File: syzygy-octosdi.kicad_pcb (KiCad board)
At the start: 2 copper layers, 50 x 100 mm, 211 parts, among them CN1 QTH-020-01-F-D-DP-A, J1 Conn_Coaxial, J2 Conn_Coaxial, J3 Conn_Coaxial, J4 Conn_Coaxial, J5 Conn_Coaxial, J6 Conn_Coaxial, J7 Conn_Coaxial, J8 Conn_Coaxial, J9 Conn_02x03_Odd_Even, U1 LMH0344SQE_NOPB, U10 GS2988-INE3, U11 STM32G031G8Ux, U2 LMH0344SQE_NOPB, U3 LMH0344SQE_NOPB, U4 LMH0344SQE_NOPB, U5 PCAL6416AHF, U6 PCAL6416AHF, U7 GS2988-INE3, U8 GS2988-INE3, U9 GS2988-INE3, X1 SX7DF148_500B20F30DNN

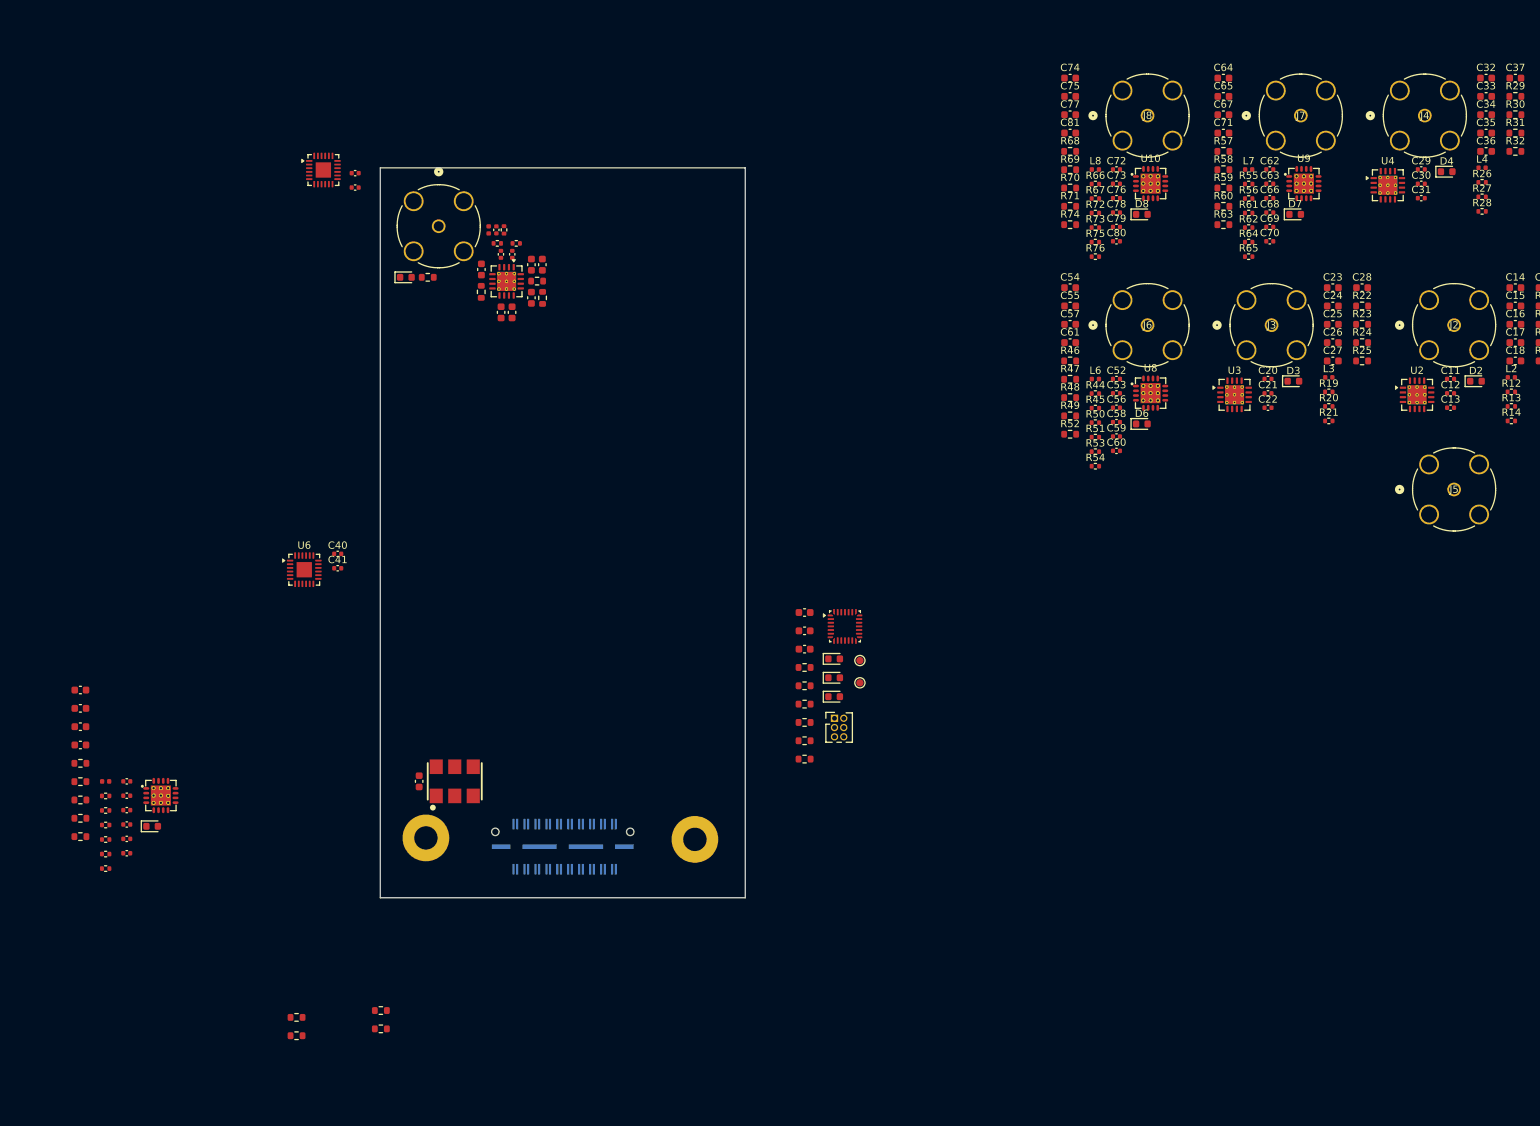
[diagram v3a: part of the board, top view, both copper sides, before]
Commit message: start laying out channels
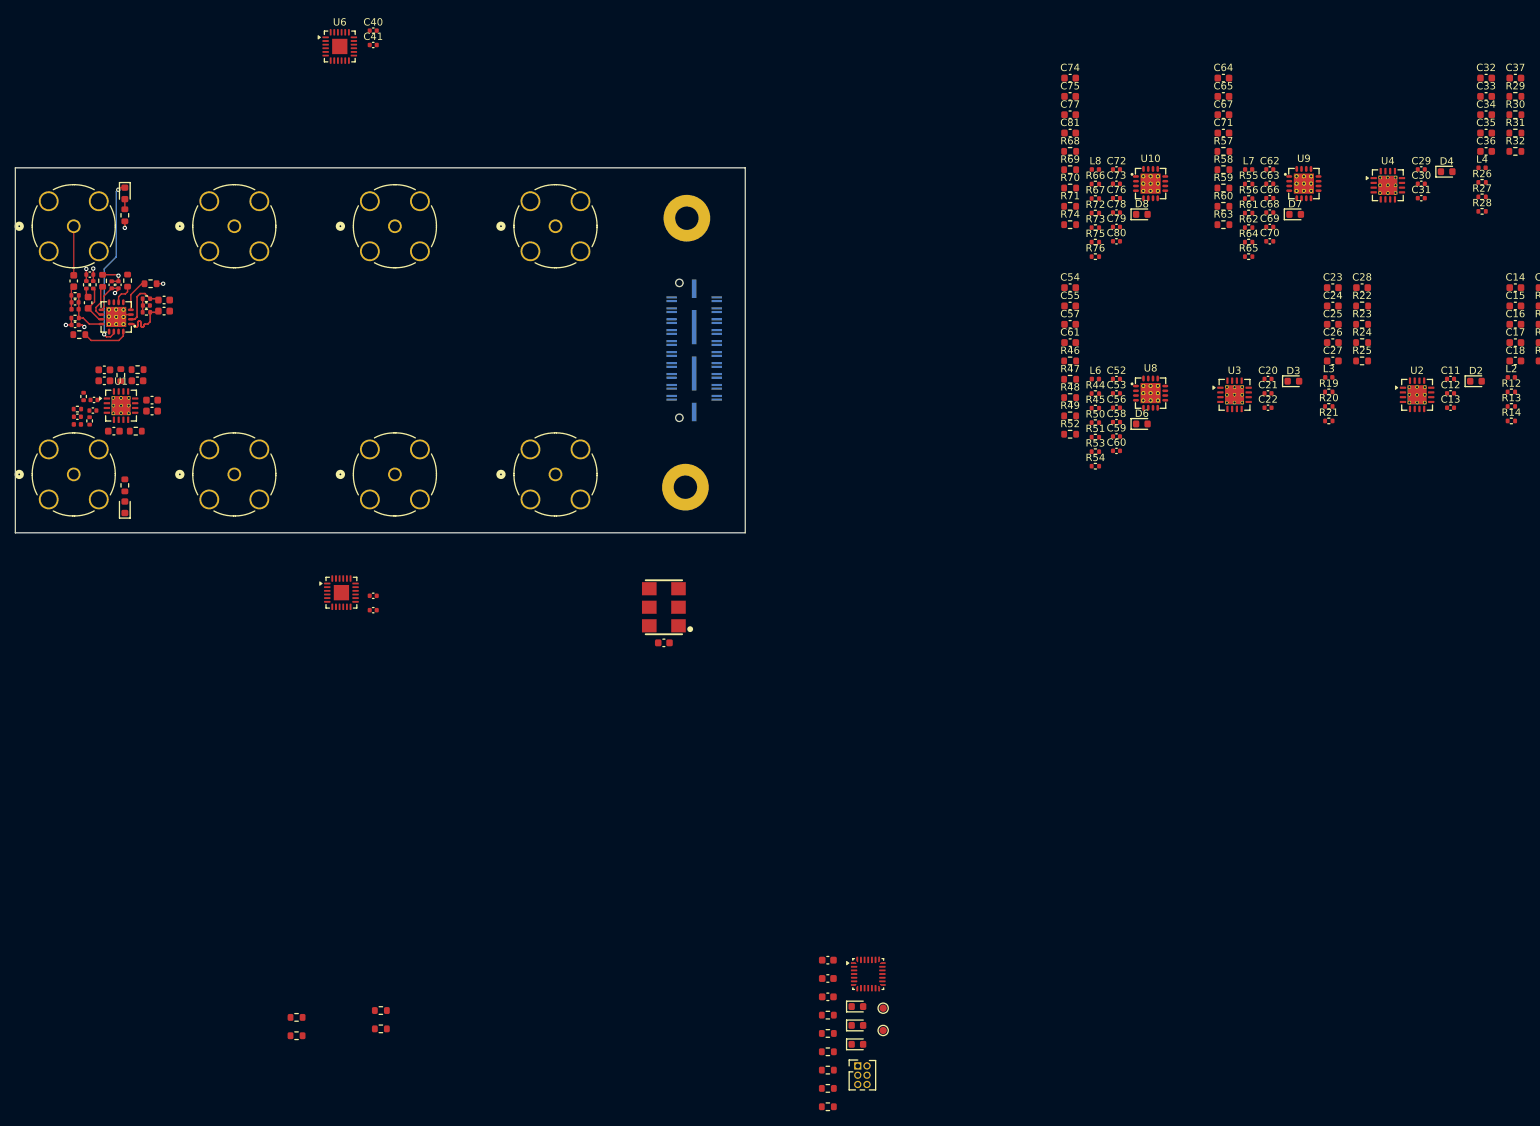
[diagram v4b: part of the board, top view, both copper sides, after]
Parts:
- removed the J8 at (205.1, 42.8)
- added J1: Conn_Coaxial, JLCImport:CONN_73171-1900_MOL, F.Cu at (58.0, 92.0)
- U1, U2, U3, U4: footprint Package_DFN_QFN:Texas_RUM0016A_WQFN-16-1EP_4x4mm_P0.65mm_EP2.6x2.6mm_ThermalVias -> JLCImport:WQFN-16-1EP_4x4mm_P0.65mm_EP2.6x2.6mm_ThermalVias
- moved J5 192.5 mm to (58.0, 58.0)
- moved J2 168.4 mm to (80.0, 92.0)
- moved J4 128.8 mm to (124.0, 92.0)
- moved J6 125.8 mm to (80.0, 58.0)
- moved J7 125.0 mm to (102.0, 58.0)
- moved J3 121.8 mm to (102.0, 92.0)
- moved D5 86.8 mm to (65.0, 53.5), turned to -90 degrees
- moved H2 85.1 mm to (142.0, 56.9), turned to 90 degrees
- moved R34 78.3 mm to (68.0, 67.9)
- moved R35 77.8 mm to (65.0, 56.5), turned to 90 degrees
- moved R41 76.4 mm to (65.4, 65.5), turned to -90 degrees
- moved C46 75.1 mm to (68.0, 68.9)
- moved R43 74.7 mm to (58.2, 67.5), turned to 180 degrees
- moved R33 74.4 mm to (68.0, 69.8), turned to 180 degrees
- moved C50 73.8 mm to (58.2, 68.4), turned to 180 degrees
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- renumbered J1 to J8
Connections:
- net Net-(U10-DDI) renamed /Outputs/SDI Out 4/DDI+
- net Net-(U10-~{DDI}) renamed /Outputs/SDI Out 4/DDI-
- net Net-(U7-DDI) renamed /Outputs/SDI Out 1/DDI+
- net Net-(U7-~{DDI}) renamed /Outputs/SDI Out 1/DDI-
- net Net-(U8-DDI) renamed /Outputs/SDI Out 2/DDI+
- net Net-(U8-~{DDI}) renamed /Outputs/SDI Out 2/DDI-
- net Net-(U9-DDI) renamed /Outputs/SDI Out 3/DDI+
- net Net-(U9-~{DDI}) renamed /Outputs/SDI Out 3/DDI-
- J8 pad 1: Net-(J1-In) -> Net-(J8-In)
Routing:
- net /Outputs/SDI Out 1/~{OSP}: track 0.00 -> 23.5 mm, vias 0 -> 2
- net +3V3: track 0.00 -> 10.5 mm, vias 0 -> 5
- net GND: track 0.00 -> 7.63 mm, vias 0 -> 3
- net /Outputs/SDI Out 1/DDI-: track 0.00 -> 7.23 mm
- net /Outputs/SDI Out 1/DDI+: track 0.00 -> 7.17 mm
- net Net-(J5-In): track 0.00 -> 6.72 mm
- net Net-(U7-SDO): track 0.00 -> 6.56 mm
- net /Outputs/SDI Out 1/~{EQ_EN}: track 0.00 -> 6.39 mm
- net Net-(U7-~{SDO}): track 0.00 -> 5.61 mm
- net /Outputs/SDI Out 1/SD/~{HD}: track 0.00 -> 4.65 mm
- net Net-(U7-REST): track 0.00 -> 4.57 mm
- net Net-(C50-Pad2): track 0.00 -> 3.24 mm
- net /Outputs/SDI Out 1/~{DISABLE}: track 0.00 -> 2.98 mm
- net Net-(C46-Pad1): track 0.00 -> 1.87 mm
- net Net-(D5-A): track 0.00 -> 1.39 mm
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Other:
- board size 50 x 100 mm -> 100 x 50 mm
- copper layers 2 -> 4

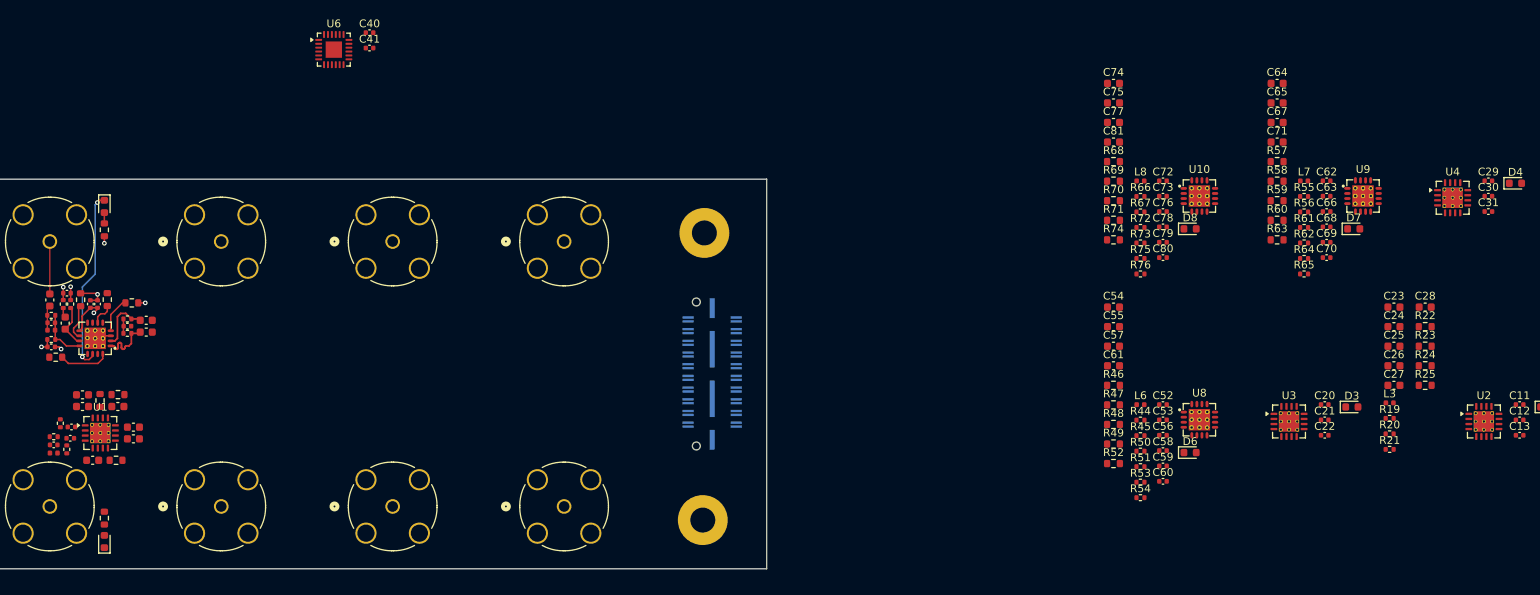
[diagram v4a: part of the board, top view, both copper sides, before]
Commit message: finish layout of first in and out channel
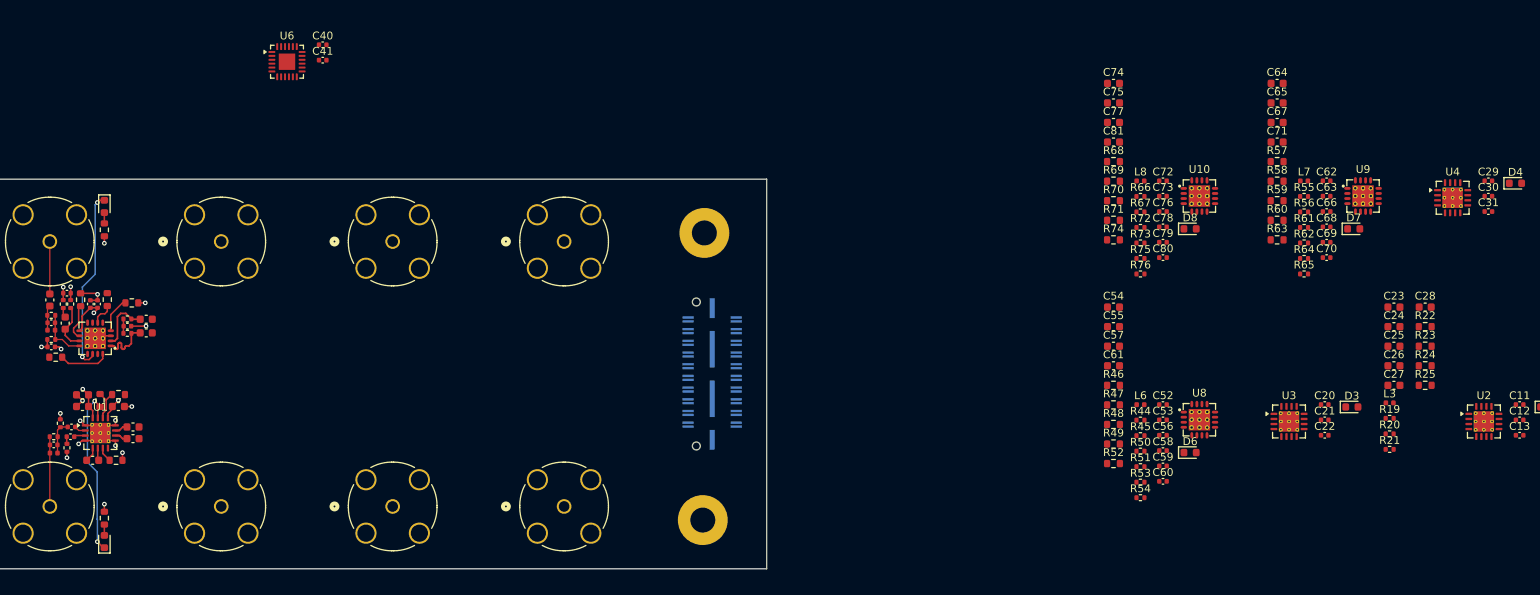
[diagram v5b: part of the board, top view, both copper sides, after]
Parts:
- U1, U2, U3, U4: footprint JLCImport:WQFN-16-1EP_4x4mm_P0.65mm_EP2.6x2.6mm_ThermalVias -> Package_DFN_QFN:Texas_RUM0016A_WQFN-16-1EP_4x4mm_P0.65mm_EP2.6x2.6mm_ThermalVias
- moved C40 6.21 mm to (93.0, 32.8)
- moved C41 6.21 mm to (93.0, 34.7)
- moved U6 6.21 mm to (88.4, 34.9)
- moved R7 0.20 mm to (60.2, 84.5)
- moved C4 0.20 mm to (60.6, 83.0)
- moved C45 0.14 mm to (70.4, 68.0)
- moved C44 0.10 mm to (70.4, 69.7)
- moved R10 0.07 mm to (66.8, 77.6)
- moved C10 0.07 mm to (66.8, 79.2)
- moved C6 0.06 mm to (68.7, 81.8)
- moved C7 0.06 mm to (68.7, 83.3)
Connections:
- net Net-(U1-SDO#) renamed /Inputs/SDI In 1/SDO-
- net Net-(U1-SDO) renamed /Inputs/SDI In 1/SDO+
- net Net-(U2-SDO#) renamed /Inputs/SDI In 2/SDO-
- net Net-(U2-SDO) renamed /Inputs/SDI In 2/SDO+
- net Net-(U3-SDO#) renamed /Inputs/SDI In 3/SDO-
- net Net-(U3-SDO) renamed /Inputs/SDI In 3/SDO+
- net Net-(U4-SDO#) renamed /Inputs/SDI In 4/SDO-
- net Net-(U4-SDO) renamed /Inputs/SDI In 4/SDO+
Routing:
- net /Inputs/SDI In 1/~{CD}: track 0.00 -> 22.8 mm, vias 0 -> 2
- net GND: track 7.63 -> 22.1 mm, vias 3 -> 13
- net Net-(J1-In): track 0.00 -> 8.95 mm
- net +3V3: track 10.5 -> 18.6 mm, vias 5 -> 8
- net /Inputs/SDI In 1/MUTE: track 0.00 -> 4.62 mm
- net Net-(C2-Pad2): track 0.00 -> 4.43 mm
- net /Inputs/SDI In 1/BYPASS: track 0.00 -> 1.92 mm
- net Net-(U1-AEC+): track 0.00 -> 1.89 mm
- net /Inputs/SDI In 1/SDO+: track 0.00 -> 1.67 mm
- net /Inputs/SDI In 1/SDO-: track 0.00 -> 1.65 mm
- net Net-(U1-AEC-): track 0.00 -> 1.61 mm
- net Net-(U1-SDI#): track 0.00 -> 1.47 mm
- net Net-(U1-SDI): track 0.00 -> 1.47 mm
- net Net-(D1-A): track 0.00 -> 1.39 mm
- net Net-(C4-Pad1): track 0.00 -> 0.93 mm
- added copper zone on In2.Cu, net +3V3
- added copper zone on In1.Cu, net GND

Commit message: route all in/out lanes
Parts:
- U1, U2, U3, U4: footprint Package_DFN_QFN:Texas_RUM0016A_WQFN-16-1EP_4x4mm_P0.65mm_EP2.6x2.6mm_ThermalVias -> JLCImport:WQFN-16-1EP_4x4mm_P0.65mm_EP2.6x2.6mm_ThermalVias
- moved L2 174.6 mm to (80.5, 85.2)
- moved R12 174.5 mm to (80.5, 83.0)
- moved R15 174.3 mm to (87.0, 93.5), turned to -90 degrees
- moved R13 173.6 mm to (81.3, 81.3), turned to 90 degrees
- moved R18 173.1 mm to (86.4, 78.4), turned to 90 degrees
- moved R14 172.8 mm to (82.2, 84.5), turned to 90 degrees
- moved R16 171.6 mm to (88.5, 86.1)
- moved C17 171.3 mm to (84.2, 77.7), turned to 180 degrees
- moved C18 171.3 mm to (84.2, 79.2), turned to 180 degrees
- moved C19 171.2 mm to (88.8, 79.2)
- moved C14 171.1 mm to (85.5, 86.1)
- moved R17 170.7 mm to (88.8, 77.6)
- moved C11 166.2 mm to (80.5, 84.1)
- moved C15 165.3 mm to (90.7, 81.8)
- moved C16 165.3 mm to (90.7, 83.3)
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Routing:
- net /TX0.P: track 0.00 -> 80.9 mm, vias 0 -> 3
- net /TX0.N: track 0.00 -> 80.0 mm, vias 0 -> 3
- net /RX0.P: track 0.00 -> 78.8 mm, vias 0 -> 1
- net /RX0.N: track 0.00 -> 78.8 mm, vias 0 -> 1
- net GND: track 22.1 -> 88.3 mm, vias 13 -> 52
- net /TX1.P: track 0.00 -> 61.6 mm, vias 0 -> 1
- net /TX1.N: track 0.00 -> 60.7 mm, vias 0 -> 1
- net /RX1.P: track 0.00 -> 55.9 mm, vias 0 -> 1
- net /RX1.N: track 0.00 -> 55.9 mm, vias 0 -> 1
- net +3V3: track 18.6 -> 74.4 mm, vias 8 -> 32
- net /TX2.N: track 0.00 -> 40.2 mm, vias 0 -> 1
- net /TX2.P: track 0.00 -> 38.5 mm, vias 0 -> 1
- net /RX2.P: track 0.00 -> 30.1 mm, vias 0 -> 1
- net /RX2.N: track 0.00 -> 30.1 mm, vias 0 -> 1
- net /Outputs/SDI Out 4/~{OSP}: track 0.00 -> 23.5 mm, vias 0 -> 2
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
